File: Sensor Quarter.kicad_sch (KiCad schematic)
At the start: 18 parts, among them IC35 SS49E, IC36 SS49E, IC37 SS49E, IC38 SS49E, IC39 SS49E, IC40 SS49E, IC41 SS49E, IC42 SS49E, IC43 CD74HC4067M96, IC44 SS49E, IC45 SS49E, IC46 SS49E, IC47 SS49E, IC48 SS49E, IC49 SS49E, IC50 SS49E, IC51 SS49E

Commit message: BOM
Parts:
- IC35, IC36, IC37, IC38, IC39, IC40, IC41, IC42, IC44, IC45, IC46, IC47, IC48, IC49, IC50, IC51: DigiKey (none) -> https://www.digikey.com/short/49qj7qmv
- IC43: DigiKey (none) -> https://www.digikey.com/short/04m5555h
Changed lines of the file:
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@@
 			)
 		)
+		(property "DigiKey" "https://www.digikey.com/short/49qj7qmv"
+			(at 196.85 76.2 0)
+			(effects
+				(font
+					(size 1.27 1.27)
+				)
+				(hide yes)
+			)
+		)
 		(pin "1"
 		)
@@
 			)
 		)
+		(property "DigiKey" "https://www.digikey.com/short/49qj7qmv"
+			(at 83.82 116.84 0)
+			(effects
+				(font
+					(size 1.27 1.27)
+				)
+				(hide yes)
+			)
+		)
 		(pin "1"
 		)
@@
 			)
 		)
+		(property "DigiKey" "https://www.digikey.com/short/49qj7qmv"
+			(at 199.39 116.84 0)
+			(effects
+				(font
+					(size 1.27 1.27)
+				)
+				(hide yes)
+			)
+		)
 		(pin "1"
 		)
@@
 			)
 		)
+		(property "DigiKey" "https://www.digikey.com/short/49qj7qmv"
+			(at 97.79 76.2 0)
+			(effects
+				(font
+					(size 1.27 1.27)
+				)
+				(hide yes)
+			)
+		)
 		(pin "1"
 		)
@@
 			)
 		)
+		(property "DigiKey" ""
+			(at 167.64 80.01 0)
+			(effects
+				(font
+					(size 1.27 1.27)
+				)
+				(hide yes)
+			)
+		)
 		(pin "1"
 		)
@@
 			)
 		)
+		(property "DigiKey" "https://www.digikey.com/short/49qj7qmv"
+			(at 237.49 116.84 0)
+			(effects
+				(font
+					(size 1.27 1.27)
+				)
+				(hide yes)
+			)
+		)
 		(pin "1"
 		)
@@
 			)
 		)
+		(property "DigiKey" "https://www.digikey.com/short/49qj7qmv"
+			(at 177.8 76.2 0)
+			(effects
+				(font
+					(size 1.27 1.27)
+				)
+				(hide yes)
+			)
+		)
 		(pin "1"
 		)
@@
 			)
 		)
+		(property "DigiKey" "https://www.digikey.com/short/49qj7qmv"
+			(at 102.87 116.84 0)
+			(effects
+				(font
+					(size 1.27 1.27)
+				)
+				(hide yes)
+			)
+		)
 		(pin "1"
 		)
@@
 			)
 		)
+		(property "DigiKey" "https://www.digikey.com/short/49qj7qmv"
+			(at 218.44 116.84 0)
+			(effects
+				(font
+					(size 1.27 1.27)
+				)
+				(hide yes)
+			)
+		)
 		(pin "1"
 		)
@@
 			)
 		)
+		(property "DigiKey" "https://www.digikey.com/short/49qj7qmv"
+			(at 215.9 76.2 0)
+			(effects
+				(font
+					(size 1.27 1.27)
+				)
+				(hide yes)
+			)
+		)
 		(pin "1"
 		)
@@
 			)
 		)
+		(property "DigiKey" "https://www.digikey.com/short/49qj7qmv"
+			(at 180.34 116.84 0)
+			(effects
+				(font
+					(size 1.27 1.27)
+				)
+				(hide yes)
+			)
+		)
 		(pin "1"
 		)
@@
 			)
 		)
+		(property "DigiKey" "https://www.digikey.com/short/04m5555h"
+			(at 133.35 83.82 0)
+			(effects
+				(font
+					(size 1.27 1.27)
+				)
+				(hide yes)
+			)
+		)
 		(pin "13"
 		)
@@
 			)
 		)
+		(property "DigiKey" "https://www.digikey.com/short/49qj7qmv"
+			(at 121.92 116.84 0)
+			(effects
+				(font
+					(size 1.27 1.27)
+				)
+				(hide yes)
+			)
+		)
 		(pin "1"
 		)
@@
 			)
 		)
+		(property "DigiKey" "https://www.digikey.com/short/49qj7qmv"
+			(at 78.74 76.2 0)
+			(effects
+				(font
+					(size 1.27 1.27)
+				)
+				(hide yes)
+			)
+		)
 		(pin "1"
 		)
@@
 			)
 		)
+		(property "DigiKey" "https://www.digikey.com/short/49qj7qmv"
+			(at 116.84 76.2 0)
+			(effects
+				(font
+					(size 1.27 1.27)
+				)
+				(hide yes)
+			)
+		)
 		(pin "1"
 		)
@@
 			)
 		)
+		(property "DigiKey" "https://www.digikey.com/short/49qj7qmv"
+			(at 234.95 76.2 0)
+			(effects
+				(font
+					(size 1.27 1.27)
+				)
+				(hide yes)
+			)
+		)
 		(pin "1"
 		)
@@
 			)
 		)
+		(property "DigiKey" "https://www.digikey.com/short/49qj7qmv"
+			(at 64.77 116.84 0)
+			(effects
+				(font
+					(size 1.27 1.27)
+				)
+				(hide yes)
+			)
+		)
 		(pin "1"
 		)
@@
 				(hide yes)
 			)
+		)
+		(property "DigiKey" "https://www.digikey.com/short/49qj7qmv"
+			(at 59.69 76.2 0)
+			(effects
+				(font
+					(size 1.27 1.27)
+				)
+				(hide yes)
+			)

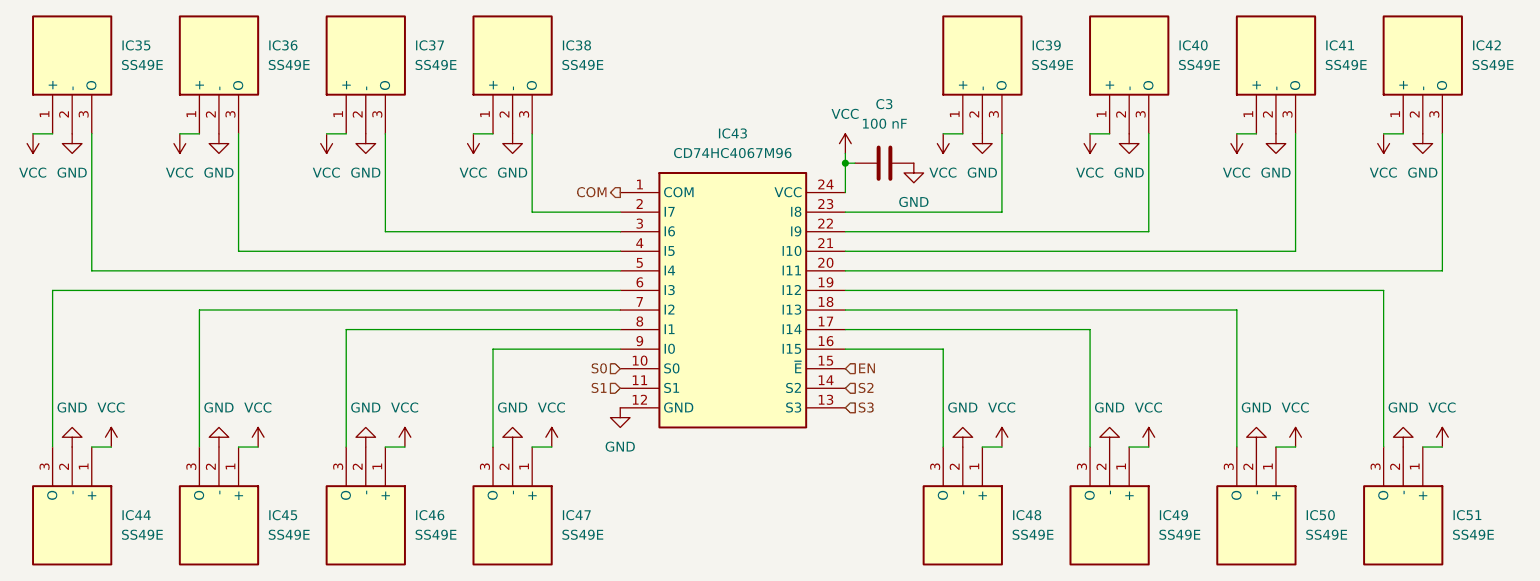
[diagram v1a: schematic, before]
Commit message: Line up linear halls
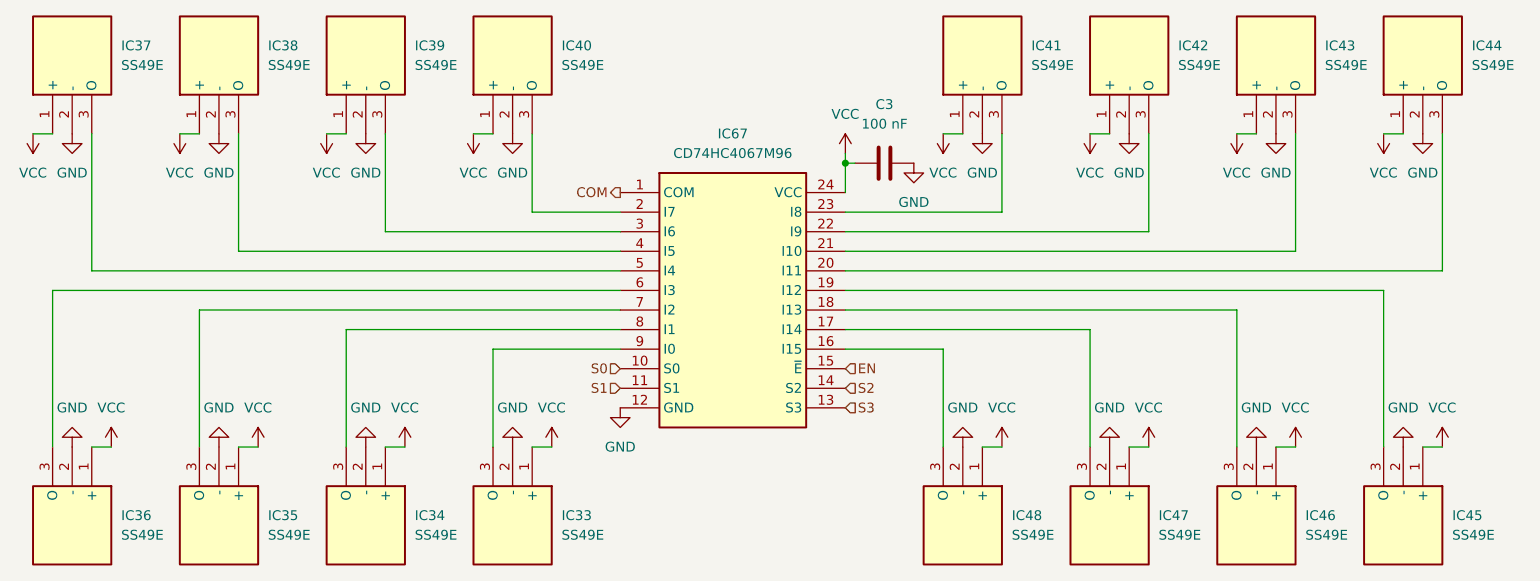
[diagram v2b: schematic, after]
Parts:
- renumbered IC47 to IC33, IC46 to IC34, IC45 to IC35, IC44 to IC36, IC35 to IC37, IC36 to IC38, IC37 to IC39, IC38 to IC40, IC39 to IC41, IC40 to IC42, IC41 to IC43, IC42 to IC44, IC51 to IC45, IC50 to IC46, IC49 to IC47, IC43 to IC67

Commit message: Redo footprint for SS49E, finish linear hall layouts
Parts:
- IC33, IC34, IC35, IC36, IC37, IC38, IC39, IC40, IC41, IC42, IC43, IC44, IC45, IC46, IC47, IC48: footprint SamacSys_PCB_Library_KiCad:TO130P160X410X300-3P -> SamacSys_PCB_Library_KiCad:SS49E
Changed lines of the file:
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@@
 			)
 		)
-		(property "Footprint" "SamacSys_PCB_Library_KiCad:TO130P160X410X300-3P"
+		(property "Footprint" "SamacSys_PCB_Library_KiCad:SS49E"
 			(at 291.77 59.69 0)
 			(effects
@@
 			)
 		)
-		(property "Footprint" "SamacSys_PCB_Library_KiCad:TO130P160X410X300-3P"
+		(property "Footprint" "SamacSys_PCB_Library_KiCad:SS49E"
 			(at -11.1 133.35 0)
 			(effects
@@
 			)
 		)
-		(property "Footprint" "SamacSys_PCB_Library_KiCad:TO130P160X410X300-3P"
+		(property "Footprint" "SamacSys_PCB_Library_KiCad:SS49E"
 			(at 104.47 133.35 0)
 			(effects
@@
 			)
 		)
-		(property "Footprint" "SamacSys_PCB_Library_KiCad:TO130P160X410X300-3P"
+		(property "Footprint" "SamacSys_PCB_Library_KiCad:SS49E"
 			(at 192.71 59.69 0)
 			(effects
@@
 			)
 		)
-		(property "Footprint" "SamacSys_PCB_Library_KiCad:TO130P160X410X300-3P"
+		(property "Footprint" "SamacSys_PCB_Library_KiCad:SS49E"
 			(at 142.57 133.35 0)
 			(effects
@@
 			)
 		)
-		(property "Footprint" "SamacSys_PCB_Library_KiCad:TO130P160X410X300-3P"
+		(property "Footprint" "SamacSys_PCB_Library_KiCad:SS49E"
 			(at 272.72 59.69 0)
 			(effects
@@
 			)
 		)
-		(property "Footprint" "SamacSys_PCB_Library_KiCad:TO130P160X410X300-3P"
+		(property "Footprint" "SamacSys_PCB_Library_KiCad:SS49E"
 			(at 7.95 133.35 0)
 			(effects
@@
 			)
 		)
-		(property "Footprint" "SamacSys_PCB_Library_KiCad:TO130P160X410X300-3P"
+		(property "Footprint" "SamacSys_PCB_Library_KiCad:SS49E"
 			(at 123.52 133.35 0)
 			(effects
@@
 			)
 		)
-		(property "Footprint" "SamacSys_PCB_Library_KiCad:TO130P160X410X300-3P"
+		(property "Footprint" "SamacSys_PCB_Library_KiCad:SS49E"
 			(at 310.82 59.69 0)
 			(effects
@@
 			)
 		)
-		(property "Footprint" "SamacSys_PCB_Library_KiCad:TO130P160X410X300-3P"
+		(property "Footprint" "SamacSys_PCB_Library_KiCad:SS49E"
 			(at 85.42 133.35 0)
 			(effects
@@
 			)
 		)
-		(property "Footprint" "SamacSys_PCB_Library_KiCad:TO130P160X410X300-3P"
+		(property "Footprint" "SamacSys_PCB_Library_KiCad:SS49E"
 			(at 27 133.35 0)
 			(effects
@@
 			)
 		)
-		(property "Footprint" "SamacSys_PCB_Library_KiCad:TO130P160X410X300-3P"
+		(property "Footprint" "SamacSys_PCB_Library_KiCad:SS49E"
 			(at 173.66 59.69 0)
 			(effects
@@
 			)
 		)
-		(property "Footprint" "SamacSys_PCB_Library_KiCad:TO130P160X410X300-3P"
+		(property "Footprint" "SamacSys_PCB_Library_KiCad:SS49E"
 			(at 211.76 59.69 0)
 			(effects
@@
 			)
 		)
-		(property "Footprint" "SamacSys_PCB_Library_KiCad:TO130P160X410X300-3P"
+		(property "Footprint" "SamacSys_PCB_Library_KiCad:SS49E"
 			(at 329.87 59.69 0)
 			(effects
@@
 			)
 		)
-		(property "Footprint" "SamacSys_PCB_Library_KiCad:TO130P160X410X300-3P"
+		(property "Footprint" "SamacSys_PCB_Library_KiCad:SS49E"
 			(at -30.15 133.35 0)
 			(effects
@@
 			)
 		)
-		(property "Footprint" "SamacSys_PCB_Library_KiCad:TO130P160X410X300-3P"
+		(property "Footprint" "SamacSys_PCB_Library_KiCad:SS49E"
 			(at 154.61 59.69 0)
 			(effects
